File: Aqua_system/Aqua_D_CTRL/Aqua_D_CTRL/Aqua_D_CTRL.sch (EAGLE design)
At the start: 234 parts, among them IC1 SN65HVD3082EDR, IC2 CSTNE8M00G520000R0, IC3 LT6106CS5#TRPBF, IC4 LT6106CS5#TRPBF, IC5 TPS54202DDCR, IC6 LD1117S33TR, IC8 LM317AEMP, J1 ESP32-PICO-KIT, K1 KB20C06A, K2 KB20C06A, Q1 DMP6185SEQ-13, Q10 BC817, Q11 2N7002, Q12 DMP6185SEQ-13, Q13 2N7002, Q14 DMP6185SEQ-13, Q15 2N7002, Q16 DMP6185SEQ-13, Q17 BC817, Q18 BC817, Q19 BC817, Q2 2N7002, Q20 BC817, Q21 BC817, Q22 BC817, Q23 BC817, Q3 DMP6185SEQ-13, Q4 2N7002, Q5 DMP6185SEQ-13, Q6 DMP6185SEQ-13, Q7 2N7002, Q8 DMP6185SEQ-13, Q9 2N7002, SW1 L101011MS02Q, U2 R7FA6M5BG3CFBLQFP_144_20X20_R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, X1 B2B-XH-AM(LF)(SN), X10 726386-2TE_726386-2, X11 282834-2, X12 RJ45-8L-B, X13 MICROMATCH-16, X14 RJ45-8L-B, X2 WF2549-2WS05S0B01, X3 282834-3, X4 282834-3, X5 726386-2TE_726386-2, X6 726386-2TE_726386-2, X7 726386-2TE_726386-2, X8 726386-2TE_726386-2, X9 726386-2TE_726386-2

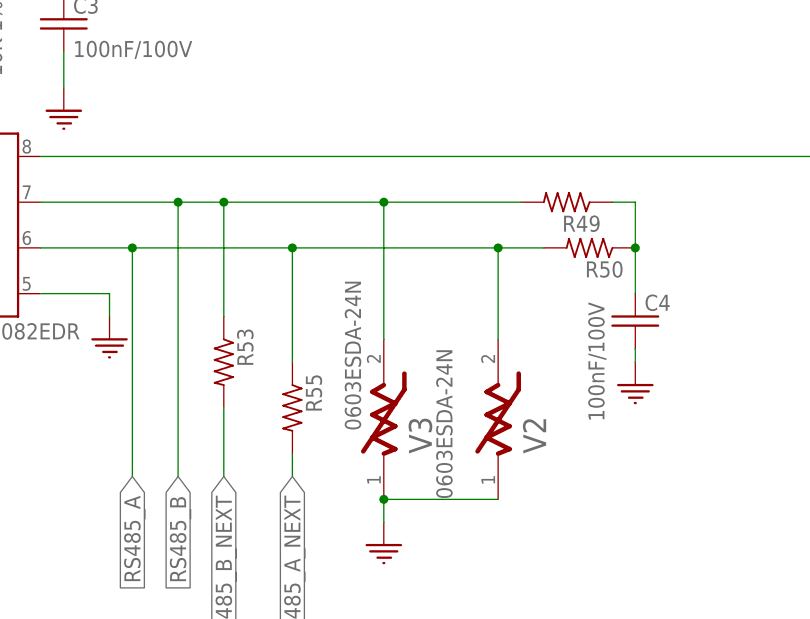
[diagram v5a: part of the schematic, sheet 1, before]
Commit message: HW01.01
Modified MCU Footprint.
Copper below ESP32-Board Chip Antenna removed.
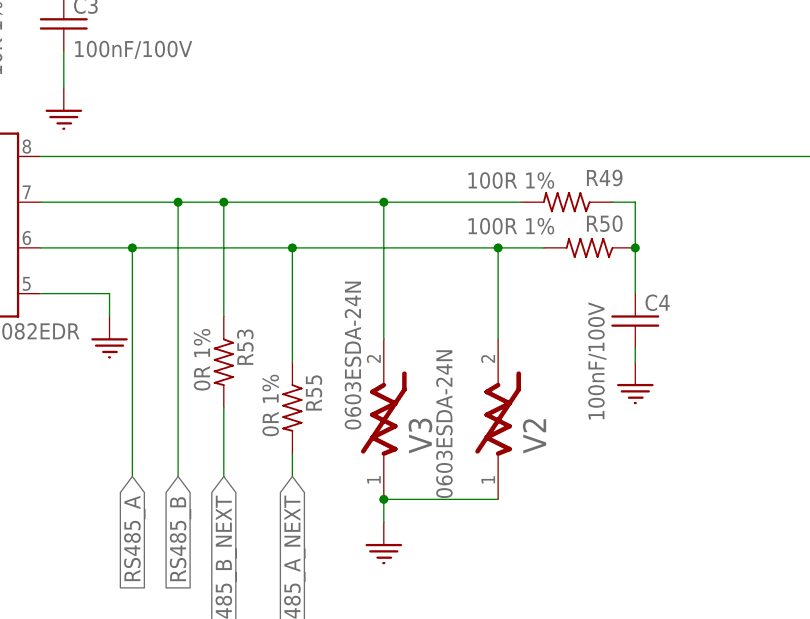
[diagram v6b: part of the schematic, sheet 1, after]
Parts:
- C67: value 1unF/50V -> 1uF/16V
- R1: value 10K -> 10K 1%
- R10, R11, R12, R2, R24, R25, R26, R3, R32, R33, R4: value (none) -> 10K 1%
- R13, R27, R49, R5, R50: value (none) -> 100R 1%
- R53, R55: value (none) -> 0R 1%
- U2: value R7FA6M5BG3CFBLQFP_144_20X20_REN-M -> R7FA6M5BG3CFBLQFP-144-M; device Labops_Lib_AH:R7FA6M5BG3CFBLQFP_144_20X20_REN-M -> Labops_Lib_AH:R7FA6M5BG3CFBLQFP-144-M
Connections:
- removed net GND1: IC2.GND
- new net N$40: R87.1, X13-12.S
- new net N$58: R89.1, X13-14.S
- net DO_BCD_A: no longer R87.1, X13-12.S
- net DO_BCD_C: no longer R89.1, X13-14.S
- net GND: now also IC2.GND
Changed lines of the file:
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@@
 <setting verticaltext="up"/>
 </settings>
-<grid distance="0.01" unitdist="inch" unit="inch" style="lines" multiple="1" display="yes" altdistance="0.01" altunitdist="inch" altunit="inch"/>
+<grid distance="0.1" unitdist="inch" unit="inch" style="lines" multiple="1" display="no" altdistance="0.01" altunitdist="inch" altunit="inch"/>
 <layers>
 <layer number="1" name="Top" color="4" fill="1" visible="no" active="no"/>
@@
 <part name="Q2" library="Labops_Lib_AH" deviceset="2N7002" device="" package3d_urn="urn:adsk.eagle:package:28738/2"/>
 <part name="GND2" library="3D_MIG_Controller" deviceset="GND" device=""/>
-<part name="R2" library="3D_MIG_Controller" deviceset="R_0603" device=""/>
-<part name="R3" library="3D_MIG_Controller" deviceset="R_0603" device=""/>
-<part name="R4" library="3D_MIG_Controller" deviceset="R_0603" device=""/>
-<part name="R5" library="3D_MIG_Controller" deviceset="R_0603" device=""/>
+<part name="R2" library="3D_MIG_Controller" deviceset="R_0603" device="" value="10K 1%"/>
+<part name="R3" library="3D_MIG_Controller" deviceset="R_0603" device="" value="10K 1%"/>
+<part name="R4" library="3D_MIG_Controller" deviceset="R_0603" device="" value="10K 1%"/>
+<part name="R5" library="3D_MIG_Controller" deviceset="R_0603" device="" value="100R 1%"/>
 <part name="Q3" library="Labops_Lib_AH" deviceset="DMP6185SEQ-13" device=""/>
 <part name="Q4" library="Labops_Lib_AH" deviceset="2N7002" device="" package3d_urn="urn:adsk.eagle:package:28738/2"/>
 <part name="GND7" library="3D_MIG_Controller" deviceset="GND" device=""/>
-<part name="R10" library="3D_MIG_Controller" deviceset="R_0603" device=""/>
-<part name="R11" library="3D_MIG_Controller" deviceset="R_0603" device=""/>
-<part name="R12" library="3D_MIG_Controller" deviceset="R_0603" device=""/>
-<part name="R13" library="3D_MIG_Controller" deviceset="R_0603" device=""/>
+<part name="R10" library="3D_MIG_Controller" deviceset="R_0603" device="" value="10K 1%"/>
+<part name="R11" library="3D_MIG_Controller" deviceset="R_0603" device="" value="10K 1%"/>
+<part name="R12" library="3D_MIG_Controller" deviceset="R_0603" device="" value="10K 1%"/>
+<part name="R13" library="3D_MIG_Controller" deviceset="R_0603" device="" value="100R 1%"/>
 <part name="FRAME2" library="frames" library_urn="urn:adsk.eagle:library:229" deviceset="A3L-LOC" device=""/>
 <part name="FRAME3" library="frames" library_urn="urn:adsk.eagle:library:229" deviceset="A3L-LOC" device=""/>
@@
 <part name="Q7" library="Labops_Lib_AH" deviceset="2N7002" device="" package3d_urn="urn:adsk.eagle:package:28738/2"/>
 <part name="GND14" library="3D_MIG_Controller" deviceset="GND" device=""/>
-<part name="R24" library="3D_MIG_Controller" deviceset="R_0603" device=""/>
-<part name="R25" library="3D_MIG_Controller" deviceset="R_0603" device=""/>
-<part name="R26" library="3D_MIG_Controller" deviceset="R_0603" device=""/>
-<part name="R27" library="3D_MIG_Controller" deviceset="R_0603" device=""/>
+<part name="R24" library="3D_MIG_Controller" deviceset="R_0603" device="" value="10K 1%"/>
+<part name="R25" library="3D_MIG_Controller" deviceset="R_0603" device="" value="10K 1%"/>
+<part name="R26" library="3D_MIG_Controller" deviceset="R_0603" device="" value="10K 1%"/>
+<part name="R27" library="3D_MIG_Controller" deviceset="R_0603" device="" value="100R 1%"/>
 <part name="R28" library="Labops_Lib_AH" deviceset="R_2010" device="">
 <attribute name="MFN" value="RL73K2HR68JTE"/>
@@
 <part name="Q9" library="Labops_Lib_AH" deviceset="2N7002" device="" package3d_urn="urn:adsk.eagle:package:28738/2"/>
 <part name="GND19" library="3D_MIG_Controller" deviceset="GND" device=""/>
-<part name="R32" library="3D_MIG_Controller" deviceset="R_0603" device=""/>
-<part name="R33" library="3D_MIG_Controller" deviceset="R_0603" device=""/>
+<part name="R32" library="3D_MIG_Controller" deviceset="R_0603" device="" value="10K 1%"/>
+<part name="R33" library="3D_MIG_Controller" deviceset="R_0603" device="" value="10K 1%"/>
 <part name="R34" library="3D_MIG_Controller" deviceset="R_0603" device="" value="10K 1%"/>
 <part name="R35" library="3D_MIG_Controller" deviceset="R_0603" device="" value="100R 1%"/>
@@
 <part name="K1" library="Labops_Lib_AH" deviceset="KB20C06A" device=""/>
 <part name="D1" library="Labops_Lib_AH" deviceset="SS14" device=""/>
-<part name="R1" library="3D_MIG_Controller" deviceset="R_0603" device="" value="10K"/>
+<part name="R1" library="3D_MIG_Controller" deviceset="R_0603" device="" value="10K 1%"/>
 <part name="GND1" library="3D_MIG_Controller" deviceset="GND" device=""/>
 <part name="V1" library="Labops_Lib_AH" deviceset="B72205S0271K101" device="" technology="B72205S2131K101"/>
@@
 <part name="R47" library="Labops_Lib_AH" deviceset="R_0603" device="" value="470R 1%"/>
 <part name="R48" library="Labops_Lib_AH" deviceset="R_0603" device="" value="470R 1%"/>
-<part name="R49" library="Labops_Lib_AH" deviceset="R_0603" device=""/>
-<part name="R50" library="Labops_Lib_AH" deviceset="R_0603" device=""/>
+<part name="R49" library="Labops_Lib_AH" deviceset="R_0603" device="" value="100R 1%"/>
+<part name="R50" library="Labops_Lib_AH" deviceset="R_0603" device="" value="100R 1%"/>
 <part name="C3" library="Labops_Lib_AH" deviceset="C_0603" device="" value="100nF/100V"/>
 <part name="GND5" library="Labops_Lib_AH" deviceset="GND" device=""/>
@@
 <part name="GND31" library="Labops_Lib_AH" deviceset="GND" device=""/>
 <part name="X12" library="con-tycoelectronics" library_urn="urn:adsk.eagle:library:193" deviceset="RJ45" device="" package3d_urn="urn:adsk.eagle:package:10660/1" technology="-8L-B"/>
-<part name="R53" library="Labops_Lib_AH" deviceset="R_0603" device=""/>
-<part name="R55" library="Labops_Lib_AH" deviceset="R_0603" device=""/>
+<part name="R53" library="Labops_Lib_AH" deviceset="R_0603" device="" value="0R 1%"/>
+<part name="R55" library="Labops_Lib_AH" deviceset="R_0603" device="" value="0R 1%"/>
 <part name="FRAME6" library="frames" library_urn="urn:adsk.eagle:library:229" deviceset="A3L-LOC" device=""/>
 <part name="R56" library="Labops_Lib_AH" deviceset="R_0603" device="" value="100R 1%"/>
@@
 <part name="GND94" library="3D_MIG_Controller" deviceset="GND" device=""/>
 <part name="GND95" library="3D_MIG_Controller" deviceset="GND" device=""/>
-<part name="C67" library="Labops_Lib_AH" deviceset="C_0603" device="" value="1unF/50V"/>
+<part name="C67" library="Labops_Lib_AH" deviceset="C_0603" device="" value="1uF/16V"/>
 <part name="C68" library="Labops_Lib_AH" deviceset="C_0603" device="" value="100nF/50V"/>
 <part name="GND97" library="3D_MIG_Controller" deviceset="GND" device=""/>
@@
 <part name="C41" library="Labops_Lib_AH" deviceset="C_0603" device="" value="100nF/50V"/>
 <part name="GND52" library="3D_MIG_Controller" deviceset="GND" device=""/>
-<part name="U2" library="Labops_Lib_AH" deviceset="R7FA6M5BG3CFB" device="LQFP_144_20X20_REN-M"/>
+<part name="U2" library="Labops_Lib_AH" deviceset="R7FA6M5BG3CFB" device="LQFP-144-M" value="R7FA6M5BG3CFBLQFP-144-M"/>
 <part name="GND53" library="3D_MIG_Controller" deviceset="GND" device=""/>
 <part name="GND54" library="3D_MIG_Controller" deviceset="GND" device=""/>
@@
 </instance>
 <instance part="R49" gate="G$1" x="165.1" y="106.68" smashed="yes" rot="R180">
-<attribute name="NAME" x="168.91" y="105.1814" size="1.778" layer="95" rot="R180"/>
-<attribute name="VALUE" x="168.91" y="109.982" size="1.778" layer="96" rot="R180"/>
+<attribute name="NAME" x="171.45" y="110.2614" size="1.778" layer="95" rot="R180"/>
+<attribute name="VALUE" x="163.83" y="109.982" size="1.778" layer="96" rot="R180"/>
 </instance>
 <instance part="R50" gate="G$1" x="167.64" y="101.6" smashed="yes" rot="R180">
-<attribute name="NAME" x="171.45" y="100.1014" size="1.778" layer="95" rot="R180"/>
-<attribute name="VALUE" x="171.45" y="104.902" size="1.778" layer="96" rot="R180"/>
+<attribute name="NAME" x="171.45" y="105.1814" size="1.778" layer="95" rot="R180"/>
+<attribute name="VALUE" x="163.83" y="104.902" size="1.778" layer="96" rot="R180"/>
 </instance>
 <instance part="C3" gate="G$1" x="109.22" y="127" smashed="yes">
@@
 <wire x1="193.04" y1="142.24" x2="203.2" y2="142.24" width="0.1524" layer="91"/>
 </segment>
+<segment>
+<pinref part="GND69" gate="1" pin="GND"/>
+<pinref part="IC2" gate="G$0" pin="GND"/>
+<wire x1="601.472" y1="142.24" x2="599.44" y2="142.24" width="0.1524" layer="91"/>
+</segment>
 </net>
 <net name="VCC" class="3">
@@
 </segment>
 </net>
-<net name="GND1" class="3">
-<segment>
-<wire x1="599.44" y1="142.24" x2="601.472" y2="142.24" width="0.1524" layer="91"/>
-<pinref part="GND69" gate="1" pin="GND"/>
-<pinref part="IC2" gate="G$0" pin="GND"/>
-</segment>
-</net>
 <net name="N$55" class="3">
 <segment>
@@
 <net name="DO_BCD_A" class="3">
 <segment>
-<pinref part="X13" gate="-12" pin="S"/>
-<wire x1="63.5" y1="96.52" x2="88.9" y2="96.52" width="0.1524" layer="91"/>
-<pinref part="R87" gate="G$1" pin="1"/>
-</segment>
-<segment>
 <wire x1="99.06" y1="96.52" x2="109.22" y2="96.52" width="0.1524" layer="91"/>
 <label x="109.22" y="96.52" size="1.778" layer="95" xref="yes"/>
@@
 <net name="DO_BCD_C" class="3">
 <segment>
-<pinref part="X13" gate="-14" pin="S"/>
-<wire x1="63.5" y1="91.44" x2="88.9" y2="91.44" width="0.1524" layer="91"/>
-<pinref part="R89" gate="G$1" pin="1"/>
-</segment>
-<segment>
 <wire x1="99.06" y1="91.44" x2="109.22" y2="91.44" width="0.1524" layer="91"/>
 <label x="109.22" y="91.44" size="1.778" layer="95" xref="yes"/>
@@
 </segment>
 </net>
+<net name="N$40" class="0">
+<segment>
+<pinref part="R87" gate="G$1" pin="1"/>
+<pinref part="X13" gate="-12" pin="S"/>
+<wire x1="88.9" y1="96.52" x2="63.5" y2="96.52" width="0.1524" layer="91"/>
+</segment>
+</net>
+<net name="N$58" class="0">
+<segment>
+<pinref part="R89" gate="G$1" pin="1"/>
+<pinref part="X13" gate="-14" pin="S"/>
+<wire x1="88.9" y1="91.44" x2="63.5" y2="91.44" width="0.1524" layer="91"/>
+</segment>
+</net>

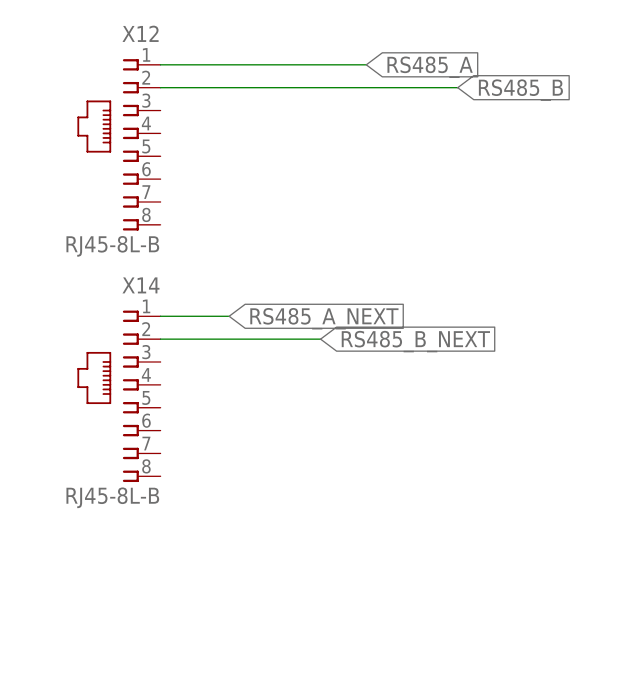
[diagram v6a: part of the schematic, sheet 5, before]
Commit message: Aqua D CTRL modification
Changed the RJ45 connectors due to limited availability of previous one
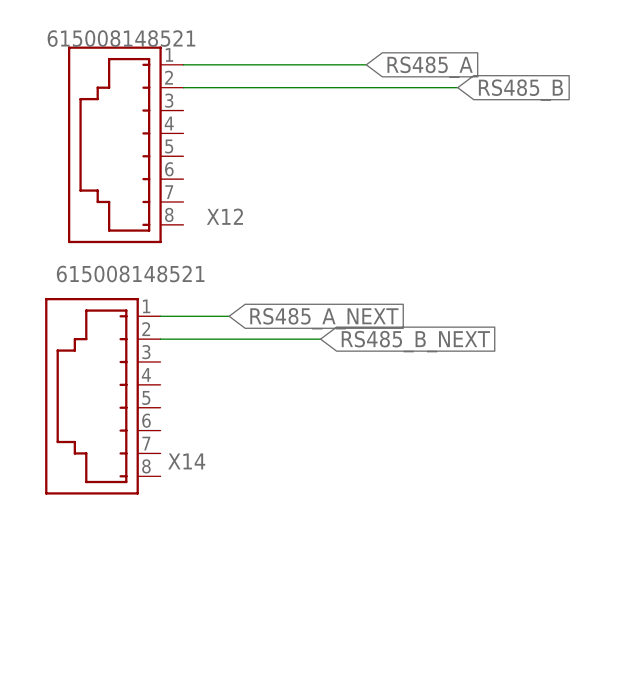
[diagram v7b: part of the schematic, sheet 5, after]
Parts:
- X12, X14: value RJ45-8L-B -> 615008148521; device con-tycoelectronics:RJ45-8L-B -> Labops_Lib_AH:615008148521
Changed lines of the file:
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@@
 <part name="X10" library="Labops_Lib_AH" deviceset="726386-2" device="TE_726386-2"/>
 <part name="GND31" library="Labops_Lib_AH" deviceset="GND" device=""/>
-<part name="X12" library="con-tycoelectronics" library_urn="urn:adsk.eagle:library:193" deviceset="RJ45" device="" package3d_urn="urn:adsk.eagle:package:10660/1" technology="-8L-B"/>
+<part name="X12" library="Labops_Lib_AH" deviceset="615008148521" device="" package3d_urn="urn:adsk.eagle:package:16446022/2"/>
 <part name="R53" library="Labops_Lib_AH" deviceset="R_0603" device="" value="0R 1%"/>
 <part name="R55" library="Labops_Lib_AH" deviceset="R_0603" device="" value="0R 1%"/>
@@
 <part name="D12" library="Labops_Lib_AH" deviceset="26-21/GPC-F3138B/CA" device=""/>
 <part name="R86" library="Labops_Lib_AH" deviceset="R_1206" device="" value="82R 1%"/>
-<part name="X14" library="con-tycoelectronics" library_urn="urn:adsk.eagle:library:193" deviceset="RJ45" device="" package3d_urn="urn:adsk.eagle:package:10660/1" technology="-8L-B"/>
+<part name="X14" library="Labops_Lib_AH" deviceset="615008148521" device="" package3d_urn="urn:adsk.eagle:package:16446022/2"/>
 <part name="R87" library="Labops_Lib_AH" deviceset="R_0603" device="" value="100R 1%"/>
 <part name="R88" library="Labops_Lib_AH" deviceset="R_0603" device="" value="100R 1%"/>
@@
 </instance>
 <instance part="GND31" gate="1" x="25.4" y="68.58" smashed="yes"/>
-<instance part="X12" gate="G$1" x="15.24" y="215.9" smashed="yes" rot="MR0">
-<attribute name="NAME" x="17.78" y="226.06" size="1.778" layer="95" rot="MR0"/>
-<attribute name="VALUE" x="17.78" y="202.692" size="1.778" layer="96" rot="MR0"/>
-</instance>
-<instance part="X14" gate="G$1" x="15.24" y="187.96" smashed="yes" rot="MR0">
-<attribute name="NAME" x="17.78" y="198.12" size="1.778" layer="95" rot="MR0"/>
-<attribute name="VALUE" x="17.78" y="174.752" size="1.778" layer="96" rot="MR0"/>
+<instance part="X12" gate="G$1" x="12.7" y="215.9" smashed="yes" rot="R90">
+<attribute name="NAME" x="22.86" y="205.74" size="1.778" layer="95"/>
+<attribute name="VALUE" x="5.08" y="225.552" size="1.778" layer="96"/>
+</instance>
+<instance part="X14" gate="G$1" x="10.16" y="187.96" smashed="yes" rot="R90">
+<attribute name="NAME" x="22.86" y="180.34" size="1.778" layer="95" rot="R180"/>
+<attribute name="VALUE" x="22.86" y="201.168" size="1.778" layer="96" rot="R180"/>
 </instance>
 <instance part="X11" gate="G$1" x="12.7" y="73.66" smashed="yes" rot="MR0">
@@
 <pinref part="X12" gate="G$1" pin="2"/>
 <label x="50.8" y="220.98" size="1.778" layer="95" xref="yes"/>
-<wire x1="17.78" y1="220.98" x2="50.8" y2="220.98" width="0.1524" layer="91"/>
+<wire x1="20.32" y1="220.98" x2="50.8" y2="220.98" width="0.1524" layer="91"/>
 </segment>
 </net>
@@
 <pinref part="X12" gate="G$1" pin="1"/>
 <label x="40.64" y="223.52" size="1.778" layer="95" xref="yes"/>
-<wire x1="40.64" y1="223.52" x2="17.78" y2="223.52" width="0.1524" layer="91"/>
+<wire x1="40.64" y1="223.52" x2="20.32" y2="223.52" width="0.1524" layer="91"/>
 </segment>
 </net>

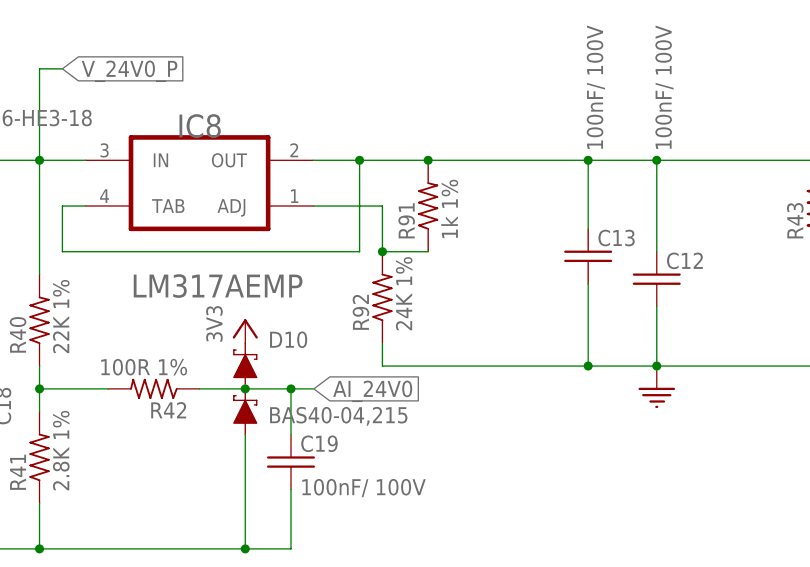
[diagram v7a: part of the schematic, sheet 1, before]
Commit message: HW01.01 Sch Change
Resistor value changed
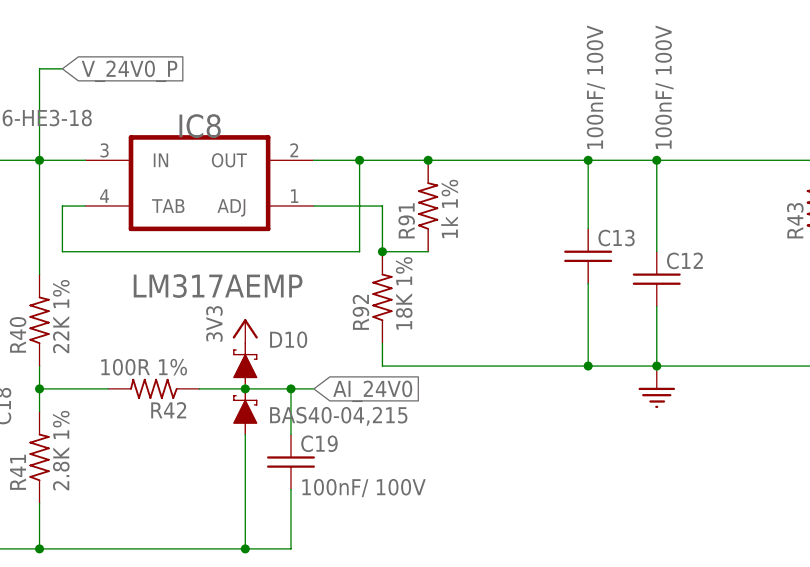
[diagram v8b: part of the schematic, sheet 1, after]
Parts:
- R92: value 24K 1% -> 18K 1%
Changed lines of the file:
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@@
 <part name="IC8" library="Labops_Lib_AH" deviceset="LM317AEMP" device=""/>
 <part name="R91" library="Labops_Lib_AH" deviceset="R_0603" device="" value="1k 1%"/>
-<part name="R92" library="Labops_Lib_AH" deviceset="R_0603" device="" value="24K 1%"/>
+<part name="R92" library="Labops_Lib_AH" deviceset="R_0603" device="" value="18K 1%"/>
 <part name="FRAME4" library="frames" library_urn="urn:adsk.eagle:library:229" deviceset="FRAME_D_L" device=""/>
 <part name="J1" library="Labops_Lib_AH" deviceset="ESP32-PICO-KIT" device=""/>
